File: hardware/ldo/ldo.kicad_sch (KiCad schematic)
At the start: 8 parts, among them U1 AMS1117-3.3

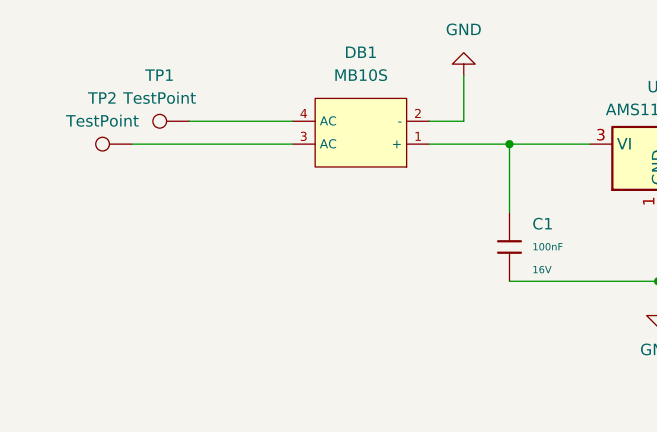
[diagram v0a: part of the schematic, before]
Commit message: repalce ldo and diode bridge
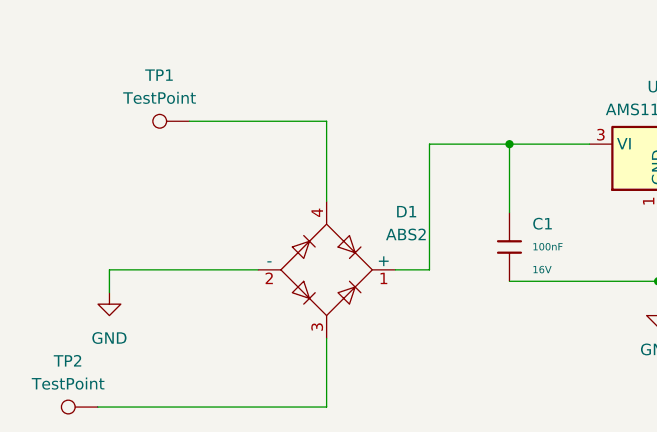
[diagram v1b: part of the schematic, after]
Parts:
- removed DB1: MB10S, PCM_JLCPCB:MBS_L4.7-W3.8-P2.40-LS7.0-TL, symbol PCM_JLCPCB-Diode-Packages:Bridge Rectifier, MB10S
- added D1: ABS2, Diode_SMD:Diode_Bridge_Diotec_ABS, symbol Diode_Bridge:ABS2
- U1: footprint Package_TO_SOT_SMD:SOT-223-3_TabPin2 -> Package_TO_SOT_SMD:SOT-89-3; LCSC Part # (none) -> C7473143
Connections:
- net GND: now also D1.2 (-)
- net at C1.1, U1.3 (VI): now also D1.1 (+)
- net at TP2.1: now also D1.3
- net at TP1.1: now also D1.4
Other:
- moved on the sheet: TP2

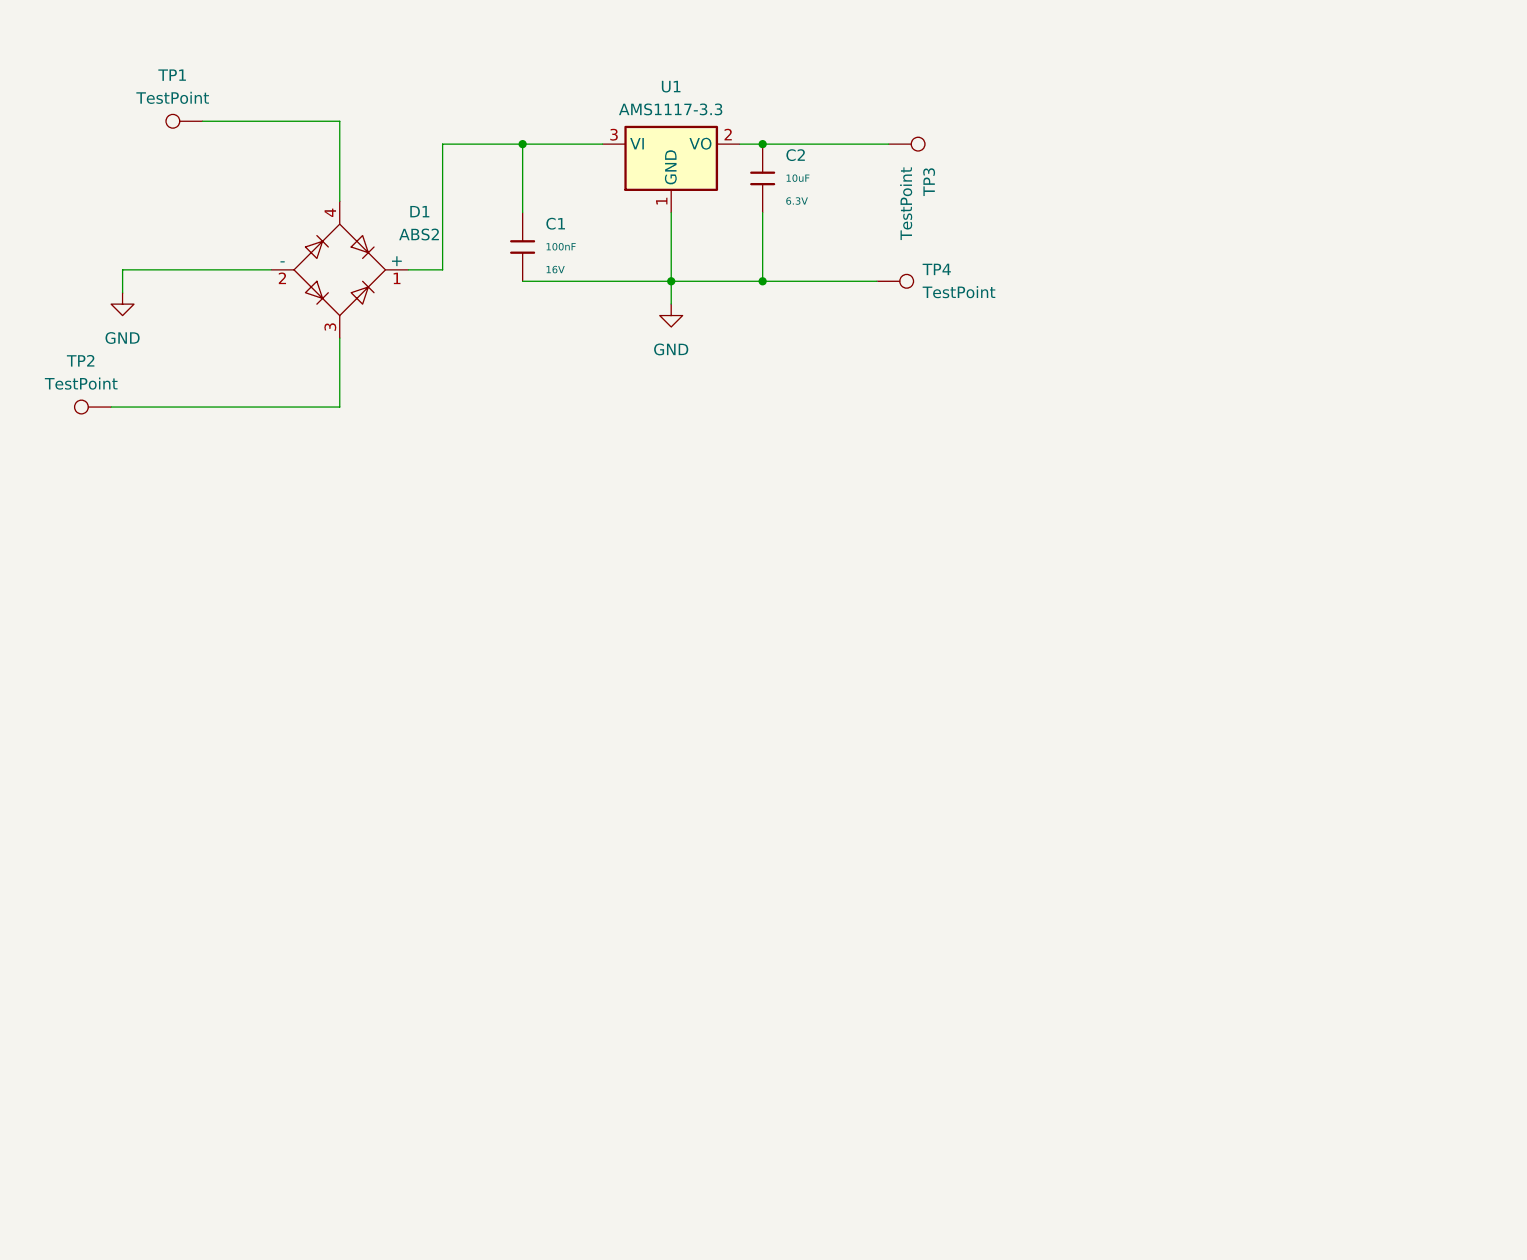
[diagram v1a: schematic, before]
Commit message: add motor driver wip
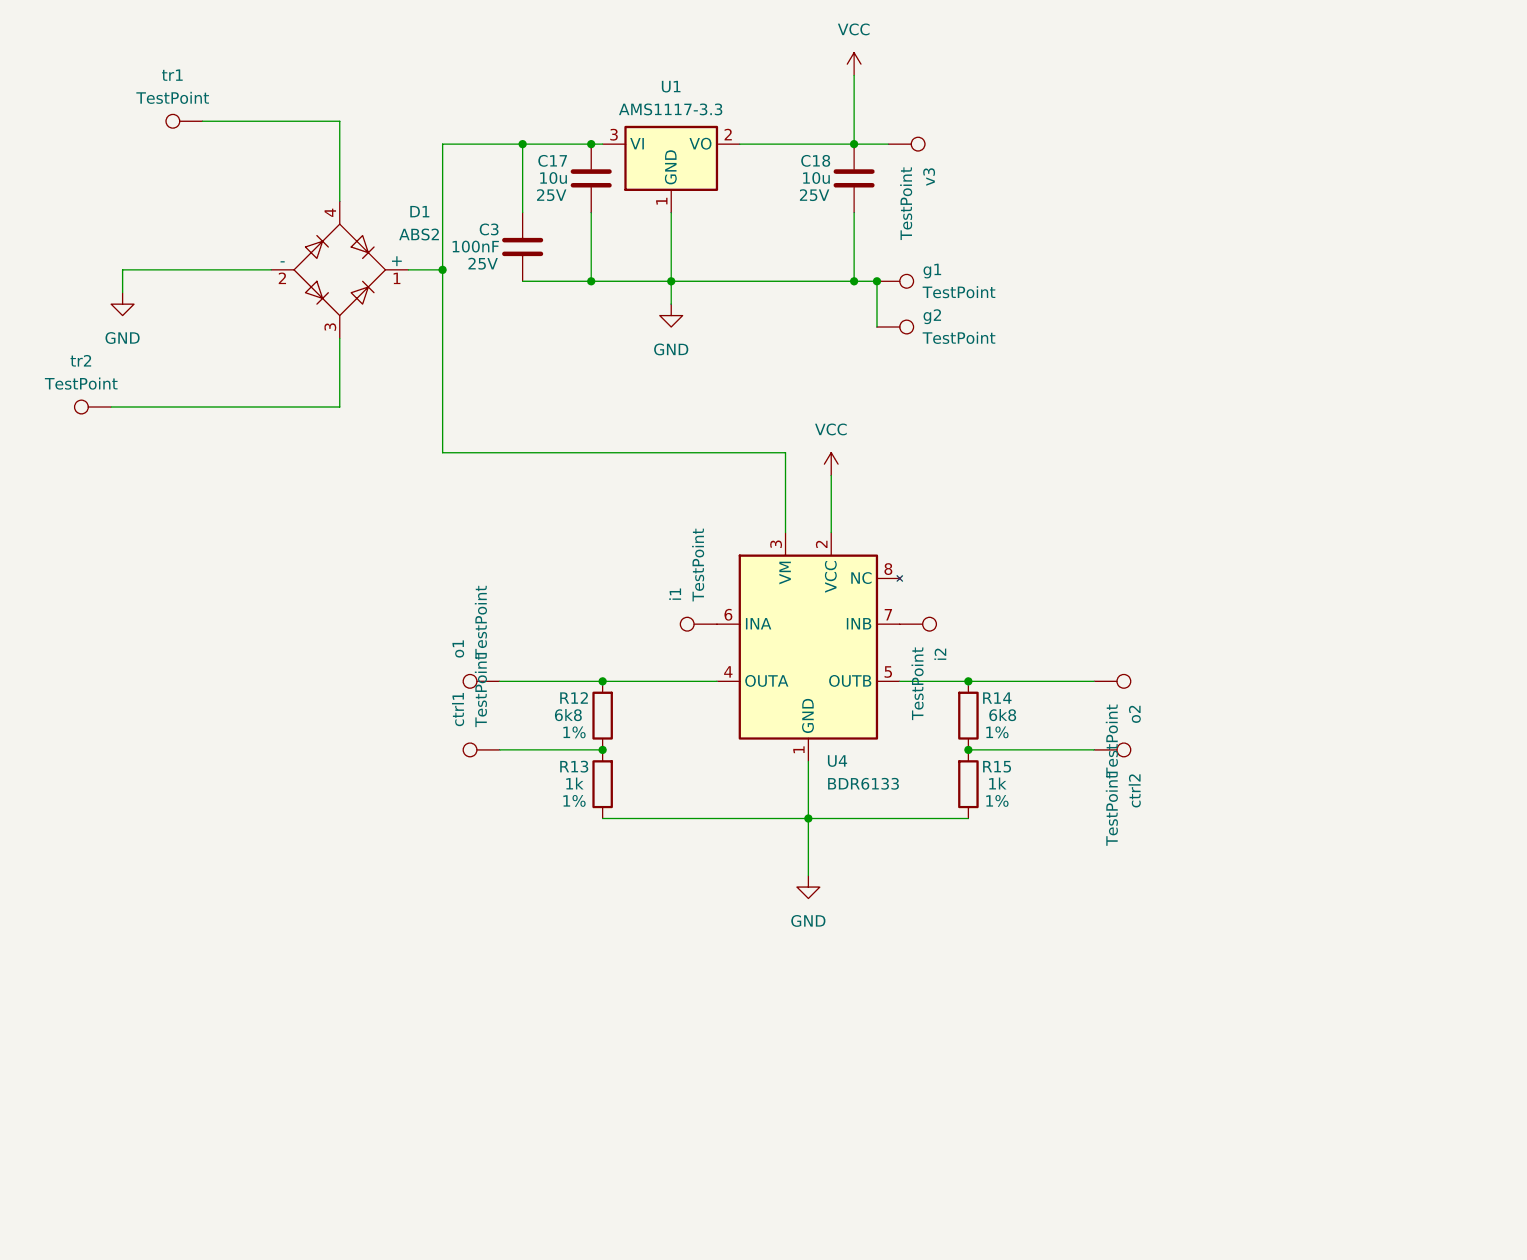
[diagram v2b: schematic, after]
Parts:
- removed C1: 100nF, PCM_JLCPCB:C_0402, symbol PCM_JLCPCB-Capacitors:0402,100nF
- removed C2: 10uF, PCM_JLCPCB:C_0402, symbol PCM_JLCPCB-Capacitors:0402,10uF
- added C17, C18: 10u, Capacitor_SMD:C_0603_1608Metric, symbol Device:C
- added C3: 100nF, Capacitor_SMD:C_0603_1608Metric, symbol Device:C
- added R12, R14: 6k8, Resistor_SMD:R_0402_1005Metric, symbol Device:R
- added R13, R15: 1k, Resistor_SMD:R_0402_1005Metric, symbol Device:R
- added U4: BDR6133, Library:SOIC-8-1EP_3.9x4.9mm_P1.27mm_EP2.41x3.3mm_ThermalVias, symbol RP2040-Decoder_Additional_Symbols:BDR6133
- added ctrl1, ctrl2, g2, i1, i2, o1, o2: TestPoint, TestPoint:TestPoint_THTPad_1.5x1.5mm_Drill0.7mm, symbol Connector:TestPoint
- renumbered TP4 to g1, TP1 to tr1, TP2 to tr2, TP3 to v3
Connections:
- net GND: now also C17.2, C18.2, C3.2, R13.1, R15.1, U4.1 (GND), U4.9 (GND), g2.1
- net VCC: now reaches U1.2 (VO), v3.1
- net VCC: now also C18.1, U4.2 (VCC)
- net at D1.1 (+), U1.3 (VI): now also C17.1, C3.1, U4.3 (VM)
- new net: R12.1, R13.2, ctrl1.1
- new net: R12.2, U4.4 (OUTA), o1.1
- new net: R14.1, R15.2, ctrl2.1
- new net: R14.2, U4.5 (OUTB), o2.1
- new net: U4.7 (INB), i2.1
- new net: U4.6 (INA), i1.1

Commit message: ams1117 + jst sh
TODO:
 - jst 1.5mm
 - TPS629210DRLR
 - esp32
 - led driver
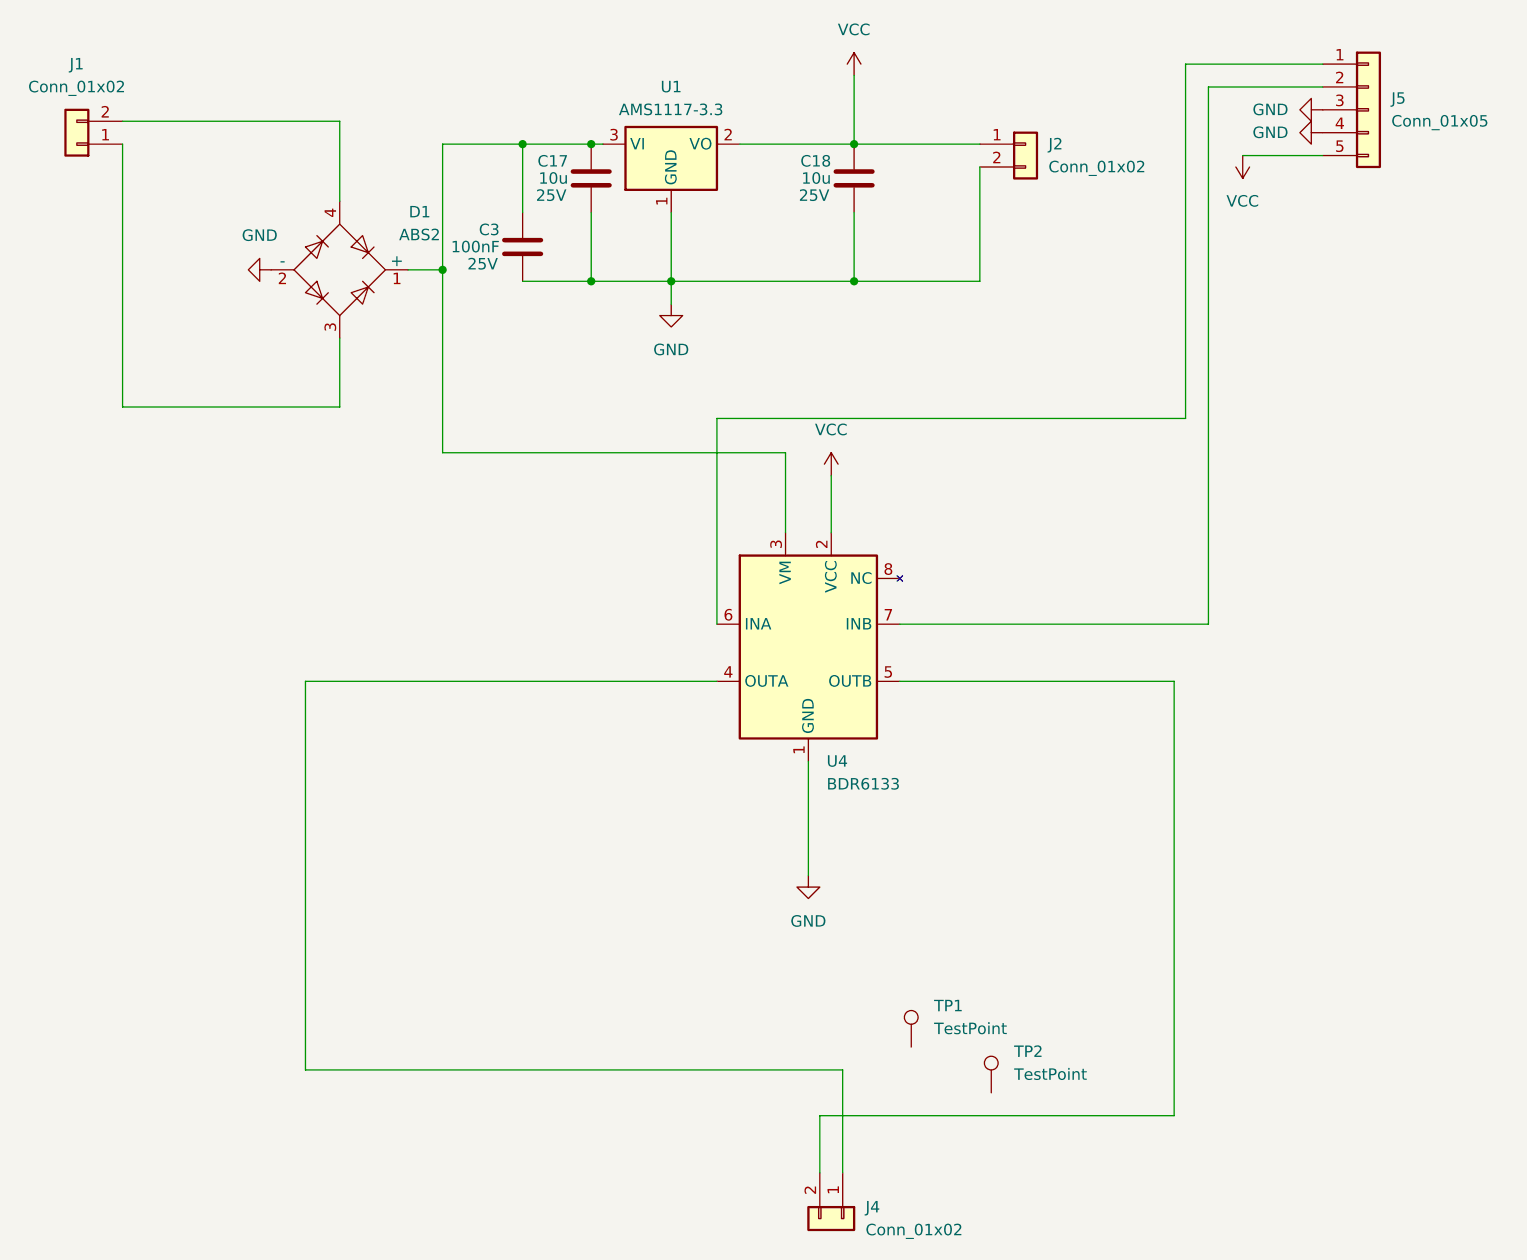
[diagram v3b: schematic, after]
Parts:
- removed R12, R14: 6k8, Resistor_SMD:R_0402_1005Metric, symbol Device:R
- removed R13, R15: 1k, Resistor_SMD:R_0402_1005Metric, symbol Device:R
- removed ctrl1, ctrl2, g1, g2, i1, i2, o1, o2, tr1, tr2, v3: TestPoint, TestPoint:TestPoint_THTPad_1.5x1.5mm_Drill0.7mm, symbol Connector:TestPoint
- added J1, J2, J4: Conn_01x02, Connector_JST:JST_SHL_SM02B-SHLS-TF_1x02-1MP_P1.00mm_Horizontal, symbol Connector_Generic:Conn_01x02
- added J5: Conn_01x05, Connector_JST:JST_SHL_SM05B-SHLS-TF_1x05-1MP_P1.00mm_Horizontal, symbol Connector_Generic:Conn_01x05
- added TP1, TP2: TestPoint, MountingHole:MountingHole_2.1mm, symbol Connector:TestPoint
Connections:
- net GND: now also J2.2 (Pin_2), J5.3 (Pin_3), J5.4 (Pin_4)
- net VCC: now also J2.1 (Pin_1), J5.5 (Pin_5)
- net at U4.4 (OUTA): now also J4.1 (Pin_1)
- net at D1.3: now also J1.1 (Pin_1)
- net at D1.4: now also J1.2 (Pin_2)
- net at U4.5 (OUTB): now also J4.2 (Pin_2)
- net at U4.7 (INB): now also J5.2 (Pin_2)
- net at U4.6 (INA): now also J5.1 (Pin_1)
